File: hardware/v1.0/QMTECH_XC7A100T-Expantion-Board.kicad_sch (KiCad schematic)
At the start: 3 parts, among them J1 Conn_01x34, J6 Conn_01x34

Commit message: backup
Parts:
- added J1: Micro_SD_Card_Det1, symbol Connector:Micro_SD_Card_Det1
- added J3: USB_C_Receptacle_USB2.0_16P, symbol Connector:USB_C_Receptacle_USB2.0_16P
- added R1, R2, R3, R4, R5, R6, R7: 4.7K, Resistor_SMD:R_0603_1608Metric_Pad0.98x0.95mm_HandSolder, symbol Device:R_Small
- added U2: CP2102N-Axx-xQFN24, Package_DFN_QFN:QFN-24-1EP_4x4mm_P0.5mm_EP2.6x2.6mm, symbol Interface_USB:CP2102N-Axx-xQFN24
- renumbered J1 to J2, J6 to J4
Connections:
- net GND: now also U1.1 (GND), U1.125 (GND), U1.126 (GND), U1.2 (GND), U1.5 (GND), U1.6 (GND), U1.61 (GND), U1.62 (GND), U1.65 (GND), U1.66 (GND), U1.69 (GND), U1.70 (GND), J1.10 (SHIELD), J1.6 (VSS), J3.A1 (GND), J3.A12 (GND), J3.B1 (GND), J3.B12 (GND), J3.S1 (SHIELD)
- new net: U2.2 (GND), U2.25 (GND)
- new net: J1.7 (DAT0), R5.2
- new net: J1.3 (CMD), R3.2
- new net: J1.2 (DAT3/CD), R2.2
- new net: J1.9 (DET), R7.2
- new net: J1.1 (DAT2), R1.2
- new net: J1.5 (CLK), R4.2
- new net: J1.8 (DAT1), R6.2
- new net: J3.A4 (VBUS), J3.A9 (VBUS), J3.B4 (VBUS), J3.B9 (VBUS)
- new net +3V3: J1.4 (VDD), R1.1, R2.1, R3.1, R4.1, R5.1, R6.1, R7.1
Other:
- note added: "MICRO-SD"
- note added: "USB-C"
- moved on the sheet: J2, J4, U1A, U1B

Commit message: updated project to Kicad version 9.0
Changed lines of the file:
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@@
 (kicad_sch
-	(version 20231120)
+	(version 20250114)
 	(generator "eeschema")
-	(generator_version "8.0")
+	(generator_version "9.0")
 	(paper "A4")
 	(bus_alias "PORT0"
@@
 		)
 	)
+	(rectangle
+		(start 185.42 114.3)
+		(end 282.575 164.465)
+		(stroke
+			(width 0.508)
+			(type dash)
+		)
+		(fill
+			(type none)
+		)
+	)
+	(rectangle
+		(start 210.82 14.605)
+		(end 244.475 111.76)
+		(stroke
+			(width 0.508)
+			(type dash)
+		)
+		(fill
+			(type none)
+		)
+	)
+	(rectangle
+		(start 248.92 14.605)
+		(end 282.575 111.76)
+		(stroke
+			(width 0.508)
+			(type dash)
+		)
+		(fill
+			(type none)
+		)
+	)
+	(rectangle
+		(start 15.24 113.665)
+		(end 92.075 160.02)
+		(stroke
+			(width 0.508)
+			(type dash)
+		)
+		(fill
+			(type none)
+		)
+	)
+	(text "PORT0"
+		(exclude_from_sim no)
+		(at 212.09 21.59 0)
+		(effects
+			(font
+				(size 3.048 3.048)
+				(thickness 0.6096)
+				(bold yes)
+			)
+			(justify left bottom)
+		)
+	)
+	(text "PORT1"
+		(exclude_from_sim no)
+		(at 250.19 21.59 0)
+		(effects
+			(font
+				(size 3.048 3.048)
+				(thickness 0.6096)
+				(bold yes)
+			)
+			(justify left bottom)
+		)
+	)
+	(text "MICRO-SD"
+		(exclude_from_sim no)
+		(at 16.51 120.65 0)
+		(effects
+			(font
+				(size 3.048 3.048)
+				(thickness 0.6096)
+				(bold yes)
+			)
+			(justify left bottom)
+		)
+	)
+	(text "USB-C"
+		(exclude_from_sim no)
+		(at 187.706 120.65 0)
+		(effects
+			(font
+				(size 3.048 3.048)
+				(thickness 0.6096)
+				(bold yes)
+			)
+			(justify left bottom)
+		)
+	)
 	(junction
 		(at 21.59 139.7)
@@
 		)
 	)
-	(rectangle
-		(start 185.42 114.3)
-		(end 282.575 164.465)
-		(stroke
-			(width 0.508)
-			(type dash)
-		)
-		(fill
-			(type none)
-		)
-	)
-	(rectangle
-		(start 210.82 14.605)
-		(end 244.475 111.76)
-		(stroke
-			(width 0.508)
-			(type dash)
-		)
-		(fill
-			(type none)
-		)
-	)
-	(rectangle
-		(start 248.92 14.605)
-		(end 282.575 111.76)
-		(stroke
-			(width 0.508)
-			(type dash)
-		)
-		(fill
-			(type none)
-		)
-	)
-	(rectangle
-		(start 15.24 113.665)
-		(end 92.075 160.02)
-		(stroke
-			(width 0.508)
-			(type dash)
-		)
-		(fill
-			(type none)
-		)
-	)
-	(text "PORT0"
-		(exclude_from_sim no)
-		(at 212.09 21.59 0)
-		(effects
-			(font
-				(size 3.048 3.048)
-				(thickness 0.6096)
-				(bold yes)
-			)
-			(justify left bottom)
-		)
-	)
-	(text "PORT1"
-		(exclude_from_sim no)
-		(at 250.19 21.59 0)
-		(effects
-			(font
-				(size 3.048 3.048)
-				(thickness 0.6096)
-				(bold yes)
-			)
-			(justify left bottom)
-		)
-	)
-	(text "MICRO-SD"
-		(exclude_from_sim no)
-		(at 16.51 120.65 0)
-		(effects
-			(font
-				(size 3.048 3.048)
-				(thickness 0.6096)
-				(bold yes)
-			)
-			(justify left bottom)
-		)
-	)
-	(text "USB-C"
-		(exclude_from_sim no)
-		(at 187.706 120.65 0)
-		(effects
-			(font
-				(size 3.048 3.048)
-				(thickness 0.6096)
-				(bold yes)
-			)
-			(justify left bottom)
-		)
-	)
 	(label "PORT0_RED7"
 		(at 232.41 34.29 180)
@@
 		(at 65.405 184.785)
 		(size 24.13 10.795)
+		(exclude_from_sim no)
+		(in_bom yes)
+		(on_board yes)
+		(dnp no)
 		(fields_autoplaced yes)
 		(stroke
@@
 		(at 39.37 184.785)
 		(size 24.13 10.795)
+		(exclude_from_sim no)
+		(in_bom yes)
+		(on_board yes)
+		(dnp no)
 		(fields_autoplaced yes)
 		(stroke
@@
 		(at 13.335 184.785)
 		(size 24.13 10.795)
+		(exclude_from_sim no)
+		(in_bom yes)
+		(on_board yes)
+		(dnp no)
 		(fields_autoplaced yes)
 		(stroke
@@
 		)
 	)
+	(embedded_fonts no)
 )

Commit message: changes
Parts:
- removed U2: CP2102N-Axx-xQFN24, Package_DFN_QFN:QFN-24-1EP_4x4mm_P0.5mm_EP2.6x2.6mm, symbol Interface_USB:CP2102N-Axx-xQFN24
- added FB1: ~, symbol Device:FerriteBead_Small
- added RN21: 5.1K, symbol Device:R_Pack02
- J3: footprint (none) -> Connector_USB:USB_C_Receptacle_Palconn_UTC16-G
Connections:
- net GND: now also RN21.3 (R2.2), RN21.4 (R1.2)
- net PORT0_BLUE0: now also U1.12 (B15_H26)
- net PORT0_BLUE1: now also U1.11 (B15_G26)
- net PORT0_BLUE2: now also U1.14 (B15_F23)
- net PORT0_BLUE3: now also U1.13 (B15_E23)
- net PORT0_BLUE4: now also U1.16 (B15_G22)
- net PORT0_BLUE5: now also U1.15 (B15_F22)
- net PORT0_BLUE6: now also U1.18 (B15_J25)
- net PORT0_BLUE7: now also U1.17 (B15_J26)
- net PORT0_CLK: now also U1.8 (B15_E26)
- net PORT0_DE: now also U1.10 (B15_E25)
- net PORT0_GREEN0: now also U1.20 (B15_G20)
- net PORT0_GREEN1: now also U1.19 (B15_G21)
- net PORT0_GREEN2: now also U1.22 (B15_H21)
- net PORT0_GREEN3: now also U1.21 (B15_H22)
- net PORT0_GREEN4: now also U1.24 (B15_K21)
- net PORT0_GREEN5: now also U1.23 (B15_J21)
- net PORT0_GREEN6: now also U1.26 (B14_K25)
- net PORT0_GREEN7: now also U1.25 (B14_K26)
- net PORT0_HS: now also U1.7 (B15_D26)
- net PORT0_RED0: now also U1.28 (B15_K22)
- net PORT0_RED1: now also U1.27 (B15_K23)
- net PORT0_RED2: now also U1.30 (B14_N26)
- net PORT0_RED3: now also U1.29 (B14_M26)
- net PORT0_RED4: now also U1.32 (B14_L22)
- net PORT0_RED5: now also U1.31 (B14_L23)
- net PORT0_RED6: now also U1.34 (B14_R26)
- net PORT0_RED7: now also U1.33 (B14_P26)
- net PORT0_VS: now also U1.9 (B15_D25)
- net PORT1_BLUE1: now also U1.101 (IO_L5)
- net PORT1_BLUE3: now also U1.103 (IO_M4)
- net PORT1_BLUE5: now also U1.105 (IO_N3)
- net PORT1_BLUE7: now also U1.107 (IO_M6)
- net PORT1_GREEN1: now also U1.109 (IO_K1)
- net PORT1_GREEN3: now also U1.111 (IO_R3)
- net PORT1_GREEN5: now also U1.113 (IO_T4)
- net PORT1_GREEN7: now also U1.115 (IO_P6)
- net PORT1_HS: now also U1.97 (IO_H9)
- net PORT1_RED1: now also U1.117 (IO_N3)
- net PORT1_RED3: now also U1.119 (IO_N1)
- net PORT1_RED5: now also U1.121 (IO_T2)
- net PORT1_RED7: now also U1.123 (IO_U2)
- net PORT1_VS: now also U1.99 (IO_M2)
- net V_USB: now reaches U1.127 (VIN)
- net V_USB: now also U1.128 (VIN), U1.63 (VIN), U1.64 (VIN)
- net at J3.A4 (VBUS), J3.A9 (VBUS), J3.B4 (VBUS)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: now also FB1.2
- net CC_MONIT1: now reaches J3.A5 (CC1)
- net CC_MONIT1: now also RN21.2 (R2.1)
- net CC_MONIT2: now reaches J3.B5 (CC2)
- net CC_MONIT2: now also RN21.1 (R1.1)
- no-connect marks 0 -> 6
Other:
- moved on the sheet: U1A, U1B

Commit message: changes
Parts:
- J1: footprint (none) -> C393941:TF-SMD_TF-PUSH
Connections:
- net SD_DAT0: now reaches J1.7 (DAT0), R5.2
- net SD_DAT0: now also U1.58 (B13_W25)
- net SD_CMD: now reaches J1.3 (CMD), R3.2
- net SD_CMD: now also U1.56 (B13_W21)
- net SD_DAT3: now reaches J1.2 (DAT3/CD), R2.2
- net SD_DAT3: now also U1.55 (B13_Y21)
- net SD_DET: now reaches J1.9 (DET), R7.2
- net SD_DET: now also U1.60 (B13_AB26)
- net SD_DAT2: now reaches J1.1 (DAT2), R1.2
- net SD_DAT2: now also U1.54 (B13_AB24)
- net SD_CLK: now reaches J1.5 (CLK), R4.2
- net SD_CLK: now also U1.57 (B13_Y26)
- net SD_DAT1: now reaches J1.8 (DAT1), R6.2
- net SD_DAT1: now also U1.59 (B13_AC26)
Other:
- moved on the sheet: R1, R2, R3, R4, R5, R6, R7

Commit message: backup
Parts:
- added C1: 0.1uf, symbol Device:C_Small
- added C9: 22uf, symbol Device:C_Small
- added R34: 450k, symbol Device:R_Small
- added U3: TPS25200, Package_SON:WSON-6-1EP_2x2mm_P0.65mm_EP1x1.6mm, symbol mylib:TPS25200
- R1, R2, R3, R4, R5, R6, R7: value 4.7K -> 4.7k
- RN21: value 5.1K -> 5.1k
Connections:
- net GND: now also C1.2, C9.2, U3.5 (GND), U3.7 (GND)
- net at FB1.1: now also C1.1, R34.1, U3.6 (IN)
- net CC_MONIT1: no longer names the net of J3.A5 (CC1), RN21.2 (R2.1)
- net CC_MONIT2: no longer names the net of J3.B5 (CC2), RN21.1 (R1.1)
- new net: C9.1, U3.1 (OUT)
- new net: R34.2, U3.4 (EN)
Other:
- moved on the sheet: FB1, RN21

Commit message: changes
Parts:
- removed RN21: 5.1k, symbol Device:R_Pack02
- removed U3: TPS25200, Package_SON:WSON-6-1EP_2x2mm_P0.65mm_EP1x1.6mm, symbol mylib:TPS25200
- added C17, C21: 4.7uf, symbol Device:C_Small
- added Q1: AON6411, Package_DFN_QFN:AO_DFN-8-1EP_5.55x5.2mm_P1.27mm_EP4.12x4.6mm, symbol Transistor_FET:AON6411
- added R35: 5.1k, symbol Device:R_Small
- added R38: 49.9k, symbol Device:R_Small
- added R39: 10.5k, symbol Device:R_Small
- added U14: HUSB238, Package_DFN_QFN:DFN-10-1EP_3x3mm_P0.5mm_EP1.65x2.38mm_ThermalVias, symbol mylib:HUSB238
- added U3: D3V3XA4B10LP, Package_DFN_QFN:Diodes_UDFN-10_1.0x2.5mm_P0.5mm, symbol Power_Protection:D3V3XA4B10LP
- C9: value 22uf -> 4.7uf
- R34: value 450k -> 10
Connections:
- net GND: now also C17.2, C21.2, R39.2, U14.11 (GND), U14.8 (VSET), U3.3 (VSS), U3.8 (VSS)
- net at C9.1: now also C17.1, C21.1, Q1.5 (D)
- net at R34.2: now also C1.1, U14.1 (VIN)
- net at FB1.1, R34.1: now also Q1.1 (S), Q1.2 (S), Q1.3 (S), R38.1; no longer C1.1
- net CC2: now reaches J3.B5 (CC2)
- net CC2: now also U14.5 (CC2), U3.5, U3.6 (NC)
- net CC1: now reaches J3.A5 (CC1)
- net CC1: now also U14.4 (CC1), U3.4, U3.7 (NC)
- net D+: now reaches J3.A6 (D+)
- net D+: now also J3.B6 (D+), U14.2 (D+), U3.2, U3.9 (NC)
- net D-: now reaches J3.A7 (D-)
- net D-: now also J3.B7 (D-), U14.3 (D-), U3.1, U3.10 (NC)
- new net: R39.1, U14.9 (ISET)
- new net: Q1.4 (G), R35.1, R38.2
- new net: R35.2, U14.10 (GATE)
- no-connect marks 6 -> 4
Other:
- note added: "0k->5v"
- note added: "10.5k->2A"
- moved on the sheet: C1, C9

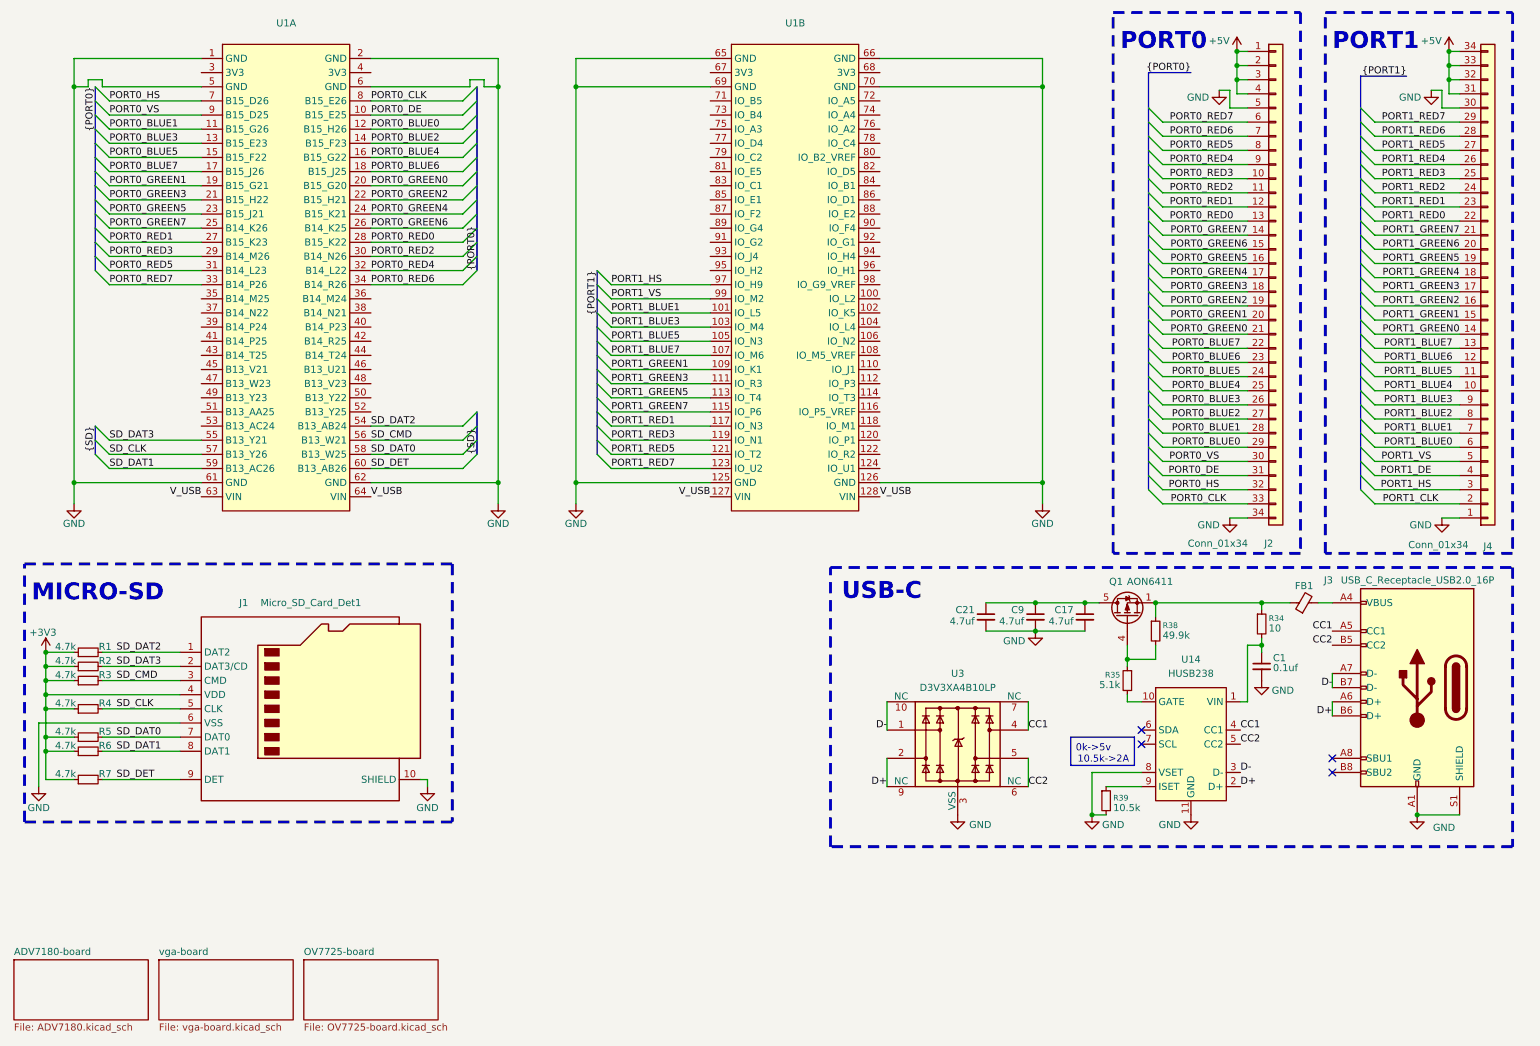
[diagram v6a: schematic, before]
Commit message: added pmod connectors instead of leds
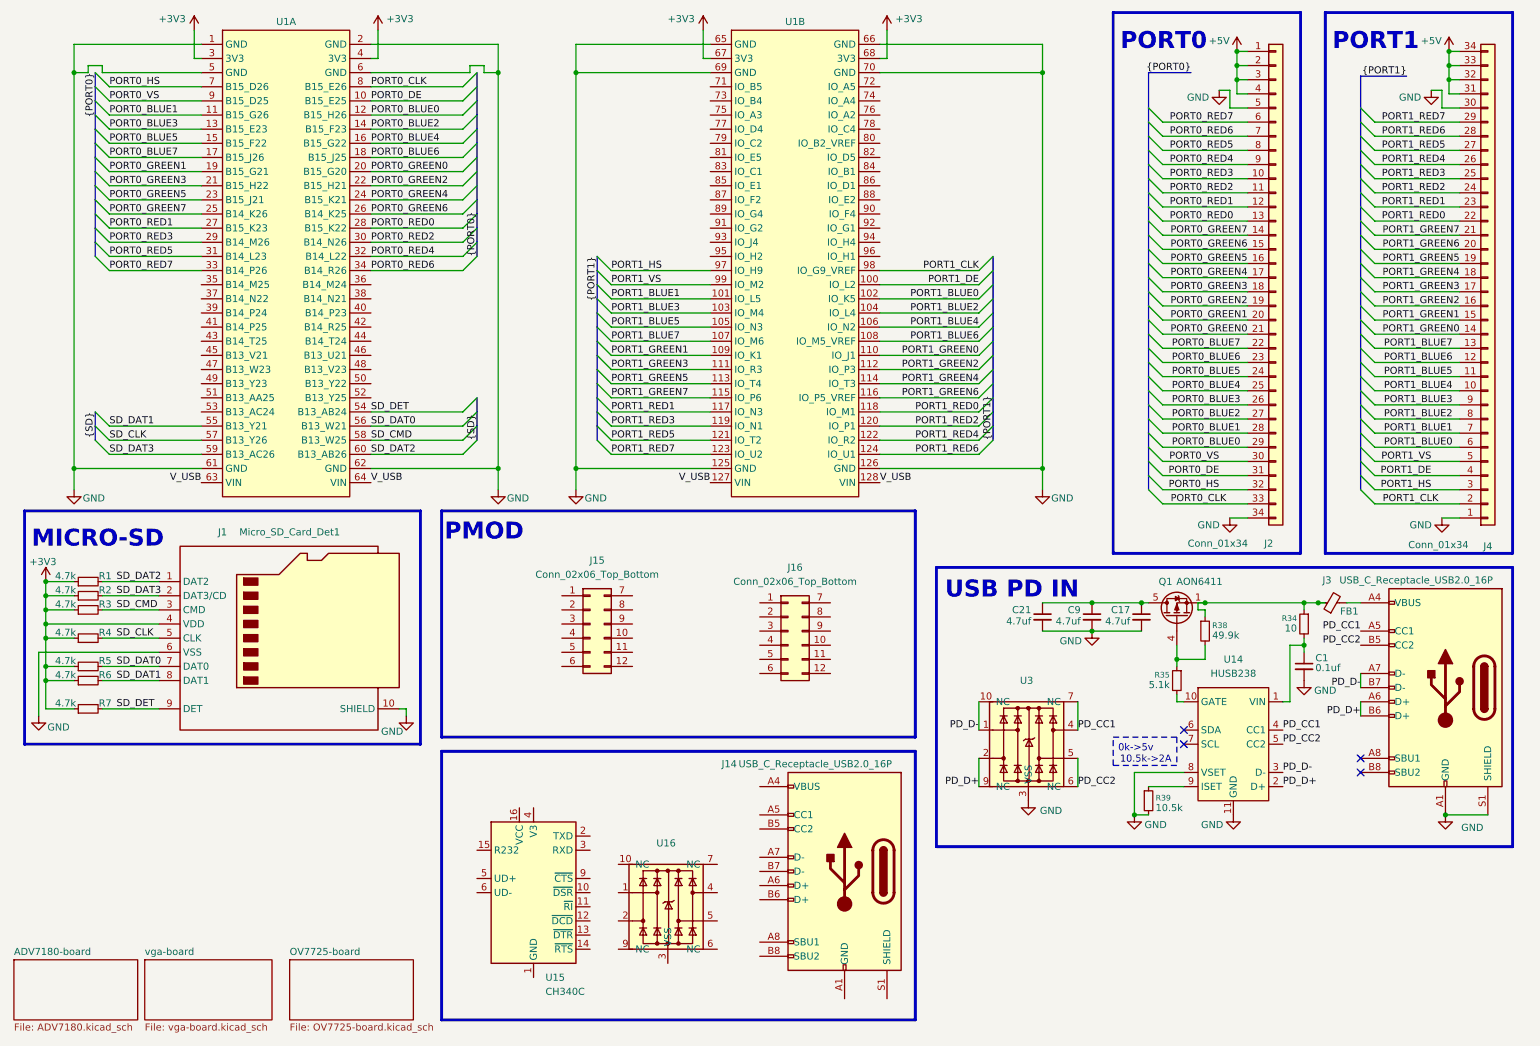
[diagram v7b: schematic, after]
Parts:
- removed U3: D3V3XA4B10LP, Package_DFN_QFN:Diodes_UDFN-10_1.0x2.5mm_P0.5mm, symbol Power_Protection:D3V3XA4B10LP
- added J14: USB_C_Receptacle_USB2.0_16P, Connector_USB:USB_C_Receptacle_Palconn_UTC16-G, symbol Connector:USB_C_Receptacle_USB2.0_16P
- added J15, J16: Conn_02x06_Top_Bottom, Connector_PinSocket_2.54mm:PinSocket_2x06_P2.54mm_Horizontal, symbol Connector_Generic:Conn_02x06_Top_Bottom
- added U15: CH340C, Package_SO:SOIC-16_3.9x9.9mm_P1.27mm, symbol Interface_USB:CH340C
- added U16, U3: ~, symbol mylib:TVS
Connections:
- net +3V3: now also U1.3 (3V3), U1.4 (3V3), U1.67 (3V3), U1.68 (3V3)
- net GND: now also U3.3 (VSS), U3.8 (VSS)
- net PORT1_BLUE0: now also U1.102 (IO_K5)
- net PORT1_BLUE2: now also U1.104 (IO_L4)
- net PORT1_BLUE4: now also U1.106 (IO_N2)
- net PORT1_BLUE6: now also U1.108 (IO_M5_VREF)
- net PORT1_CLK: now also U1.98 (IO_G9_VREF)
- net PORT1_DE: now also U1.100 (IO_L2)
- net PORT1_GREEN0: now also U1.110 (IO_J1)
- net PORT1_GREEN2: now also U1.112 (IO_P3)
- net PORT1_GREEN4: now also U1.114 (IO_T3)
- net PORT1_GREEN6: now also U1.116 (IO_P5_VREF)
- net PORT1_RED0: now also U1.118 (IO_M1)
- net PORT1_RED2: now also U1.120 (IO_P1)
- net PORT1_RED4: now also U1.122 (IO_R2)
- net PORT1_RED6: now also U1.124 (IO_U1)
- net SD_CMD: now also U1.58 (B13_W25); no longer U1.56 (B13_W21)
- net SD_DAT0: now also U1.56 (B13_W21); no longer U1.58 (B13_W25)
- net SD_DAT1: now also U1.55 (B13_Y21); no longer U1.59 (B13_AC26)
- net SD_DAT2: now also U1.60 (B13_AB26); no longer U1.54 (B13_AB24)
- net SD_DAT3: now also U1.59 (B13_AC26); no longer U1.55 (B13_Y21)
- net SD_DET: now also U1.54 (B13_AB24); no longer U1.60 (B13_AB26)
- net CC1 renamed PD_CC1
- net PD_CC1: now also U3.4, U3.7 (NC)
- net CC2 renamed PD_CC2
- net PD_CC2: now also U3.5, U3.6 (NC)
- net D+ renamed PD_D+
- net PD_D+: now also U3.2, U3.9 (NC)
- net D- renamed PD_D-
- net PD_D-: now also U3.1, U3.10 (NC)
- new net: J14.A1 (GND), J14.A12 (GND), J14.B1 (GND), J14.B12 (GND)
- new net: J14.A4 (VBUS), J14.A9 (VBUS), J14.B4 (VBUS), J14.B9 (VBUS)
- new net: U16.3 (VSS), U16.8 (VSS)
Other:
- note added: "PMOD"
- note added: "USB PD IN"
- note removed: "USB-C"
- moved on the sheet: C1, C17, C21, C9, FB1, J1, J3, Q1, R1, R2, R3, R34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
